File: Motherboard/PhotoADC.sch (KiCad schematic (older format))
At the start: 28 parts

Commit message: Moving along
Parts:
- removed D?: LED, symbol LED
- removed P?: CONN_02X12, symbol CONN_02X12
- added D501: GREEN_LED, LEDs:LED_0805, symbol LED
- added P501, P502, P503, P504: CONN_01X03, moboFootprints:3POS_Header_TEConn_6.35mm_pitch, symbol CONN_01X03
- U501: renamed from U?; footprint (none) -> Housings_SSOP:TSSOP-38_4.4x9.7mm_Pitch0.5mm
- gave numbers to parts that had none: 23
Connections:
- wire segments 58 -> 54

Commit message: Final edits -- awaiting review before sending out
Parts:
- removed C507: 1uF, symbol C
- removed C514: 10nF, symbol C
- removed C515: 2.2uF, symbol C
- removed D501: GREEN_LED, LEDs:LED_0805, symbol LED
- removed R504: 300, symbol R
- removed U503: LP2985-N, symbol LP2985-N
- U501: footprint (none) -> Housings_SSOP:TSSOP-38_4.4x9.7mm_Pitch0.5mm
- U502: footprint (none) -> TO_SOT_Packages_SMD:SOT-23-5_HandSoldering
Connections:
- net GND: now also C508.1, C509.1, C510.1, C511.1, C512.1, C513.1, U504.4 (GND)

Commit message: computer is dying
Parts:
- added R504: 0, Resistors_SMD:R_0805_HandSoldering, symbol R
- R501: footprint (none) -> Resistors_SMD:R_0805_HandSoldering
- R502: footprint (none) -> Resistors_SMD:R_0603_HandSoldering
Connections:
- net at R502.2, U502.1 (Vout): now also R504.1; no longer U502.4 (-)
- new net: R504.2, U502.4 (-)
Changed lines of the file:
@@
 MUX_DATA
 $Comp
-L GND #PWR030
+L GND #PWR513
 U 1 1 59280857
 P 9900 3050
-F 0 "#PWR030" H 9900 2800 50  0001 C CNN
+F 0 "#PWR513" H 9900 2800 50  0001 C CNN
 F 1 "GND" H 9900 2900 50  0000 C CNN
 F 2 "" H 9900 3050 50  0000 C CNN
@@
 $EndComp
 $Comp
-L +5V #PWR031
+L +5V #PWR502
 U 1 1 5928085D
 P 9900 700
-F 0 "#PWR031" H 9900 550 50  0001 C CNN
+F 0 "#PWR502" H 9900 550 50  0001 C CNN
 F 1 "+5V" H 9900 840 50  0000 C CNN
 F 2 "" H 9900 700 50  0000 C CNN
@@
 $EndComp
 $Comp
-L +5V #PWR032
+L +5V #PWR501
 U 1 1 59280863
 P 9700 700
-F 0 "#PWR032" H 9700 550 50  0001 C CNN
+F 0 "#PWR501" H 9700 550 50  0001 C CNN
 F 1 "+5V" H 9700 840 50  0000 C CNN
 F 2 "" H 9700 700 50  0000 C CNN
@@
 $EndComp
 $Comp
-L GND #PWR033
+L GND #PWR509
 U 1 1 5928087F
 P 8850 1750
-F 0 "#PWR033" H 8850 1500 50  0001 C CNN
+F 0 "#PWR509" H 8850 1500 50  0001 C CNN
 F 1 "GND" H 8850 1600 50  0000 C CNN
 F 2 "" H 8850 1750 50  0000 C CNN
@@
 $EndComp
 $Comp
-L GND #PWR034
+L GND #PWR510
 U 1 1 5928088C
 P 10650 1800
-F 0 "#PWR034" H 10650 1550 50  0001 C CNN
+F 0 "#PWR510" H 10650 1550 50  0001 C CNN
 F 1 "GND" H 10650 1650 50  0000 C CNN
 F 2 "" H 10650 1800 50  0000 C CNN
@@
 $EndComp
 $Comp
-L +5V #PWR035
+L +5V #PWR514
 U 1 1 5928089C
 P 9300 4500
-F 0 "#PWR035" H 9300 4350 50  0001 C CNN
+F 0 "#PWR514" H 9300 4350 50  0001 C CNN
 F 1 "+5V" H 9300 4640 50  0000 C CNN
 F 2 "" H 9300 4500 50  0000 C CNN
@@
 $EndComp
 $Comp
-L GND #PWR036
+L GND #PWR516
 U 1 1 592808A9
 P 9300 5350
-F 0 "#PWR036" H 9300 5100 50  0001 C CNN
+F 0 "#PWR516" H 9300 5100 50  0001 C CNN
 F 1 "GND" H 9300 5200 50  0000 C CNN
 F 2 "" H 9300 5350 50  0000 C CNN
@@
 $EndComp
 $Comp
-L GND #PWR037
+L GND #PWR515
 U 1 1 592808AF
 P 9750 4650
-F 0 "#PWR037" H 9750 4400 50  0001 C CNN
+F 0 "#PWR515" H 9750 4400 50  0001 C CNN
 F 1 "GND" H 9750 4500 50  0000 C CNN
 F 2 "" H 9750 4650 50  0000 C CNN
@@
 F 0 "R502" V 10180 4950 50  0000 C CNN
 F 1 "100" V 10100 4950 50  0000 C CNN
-F 2 "" V 10030 4950 50  0001 C CNN
+F 2 "Resistors_SMD:R_0603_HandSoldering" V 10030 4950 50  0001 C CNN
 F 3 "" H 10100 4950 50  0000 C CNN
 	1    10100 4950
@@
 F 0 "R501" V 8680 4900 50  0000 C CNN
 F 1 "0" V 8600 4900 50  0000 C CNN
-F 2 "" V 8530 4900 50  0001 C CNN
+F 2 "Resistors_SMD:R_0805_HandSoldering" V 8530 4900 50  0001 C CNN
 F 3 "" H 8600 4900 50  0000 C CNN
 	1    8600 4900
@@
 $EndComp
 $Comp
-L +5V #PWR038
+L +5V #PWR517
 U 1 1 59280900
 P 3300 6050
-F 0 "#PWR038" H 3300 5900 50  0001 C CNN
+F 0 "#PWR517" H 3300 5900 50  0001 C CNN
 F 1 "+5V" H 3300 6190 50  0000 C CNN
 F 2 "" H 3300 6050 50  0000 C CNN
@@
 NoConn ~ 6350 1750
 $Comp
-L +5V #PWR039
+L +5V #PWR507
 U 1 1 592A5C75
 P 700 1700
-F 0 "#PWR039" H 700 1550 50  0001 C CNN
+F 0 "#PWR507" H 700 1550 50  0001 C CNN
 F 1 "+5V" H 700 1840 50  0000 C CNN
 F 2 "" H 700 1700 50  0000 C CNN
@@
 $EndComp
 $Comp
-L +5V #PWR040
+L +5V #PWR503
 U 1 1 592A5D71
 P 700 1150
-F 0 "#PWR040" H 700 1000 50  0001 C CNN
+F 0 "#PWR503" H 700 1000 50  0001 C CNN
 F 1 "+5V" H 700 1290 50  0000 C CNN
 F 2 "" H 700 1150 50  0000 C CNN
@@
 $EndComp
 $Comp
-L +5V #PWR041
+L +5V #PWR508
 U 1 1 592A5DDE
 P 2550 1700
-F 0 "#PWR041" H 2550 1550 50  0001 C CNN
+F 0 "#PWR508" H 2550 1550 50  0001 C CNN
 F 1 "+5V" H 2550 1840 50  0000 C CNN
 F 2 "" H 2550 1700 50  0000 C CNN
@@
 $EndComp
 $Comp
-L +5V #PWR042
+L +5V #PWR504
 U 1 1 592A5DE5
 P 2550 1150
-F 0 "#PWR042" H 2550 1000 50  0001 C CNN
+F 0 "#PWR504" H 2550 1000 50  0001 C CNN
 F 1 "+5V" H 2550 1290 50  0000 C CNN
 F 2 "" H 2550 1150 50  0000 C CNN
@@
 Wire Wire Line
 	9100 4850 9100 4200
-Wire Wire Line
-	9100 4200 9950 4200
 Wire Wire Line
 	9950 4200 9950 4950
@@
 CH3
 $Comp
-L GND #PWR043
+L GND #PWR506
 U 1 1 592A6F6A
 P 2000 1350
-F 0 "#PWR043" H 2000 1100 50  0001 C CNN
+F 0 "#PWR506" H 2000 1100 50  0001 C CNN
 F 1 "GND" H 2000 1200 50  0000 C CNN
 F 2 "" H 2000 1350 50  0000 C CNN
@@
 $EndComp
 $Comp
-L GND #PWR044
+L GND #PWR512
 U 1 1 592A6FD0
 P 2000 1900
-F 0 "#PWR044" H 2000 1650 50  0001 C CNN
+F 0 "#PWR512" H 2000 1650 50  0001 C CNN
 F 1 "GND" H 2000 1750 50  0000 C CNN
 F 2 "" H 2000 1900 50  0000 C CNN
@@
 $EndComp
 $Comp
-L GND #PWR045
+L GND #PWR505
 U 1 1 592A70ED
 P 1150 1350
-F 0 "#PWR045" H 1150 1100 50  0001 C CNN
+F 0 "#PWR505" H 1150 1100 50  0001 C CNN
 F 1 "GND" H 1150 1200 50  0000 C CNN
 F 2 "" H 1150 1350 50  0000 C CNN
@@
 $EndComp
 $Comp
-L GND #PWR046
+L GND #PWR511
 U 1 1 592A714C
 P 1150 1900
-F 0 "#PWR046" H 1150 1650 50  0001 C CNN
+F 0 "#PWR511" H 1150 1650 50  0001 C CNN
 F 1 "GND" H 1150 1750 50  0000 C CNN
 F 2 "" H 1150 1900 50  0000 C CNN
@@
 Connection ~ 4000 6850
 $Comp
-L GND #PWR047
+L GND #PWR518
 U 1 1 595D7156
 P 4450 6850
-F 0 "#PWR047" H 4450 6600 50  0001 C CNN
+F 0 "#PWR518" H 4450 6600 50  0001 C CNN
 F 1 "GND" H 4450 6700 50  0000 C CNN
 F 2 "" H 4450 6850 50  0000 C CNN
@@
 	1    0    0    -1
 $EndComp
+$Comp
+L R R504
+U 1 1 5962A104
+P 9500 4200
+F 0 "R504" V 9580 4200 50  0000 C CNN
+F 1 "0" V 9500 4200 50  0000 C CNN
+F 2 "Resistors_SMD:R_0805_HandSoldering" V 9430 4200 50  0001 C CNN
+F 3 "" H 9500 4200 50  0000 C CNN
+	1    9500 4200
+	0    1    1    0
+$EndComp
+Wire Wire Line
+	9100 4200 9350 4200
+Wire Wire Line
+	9650 4200 9950 4200
 $EndSCHEMATC

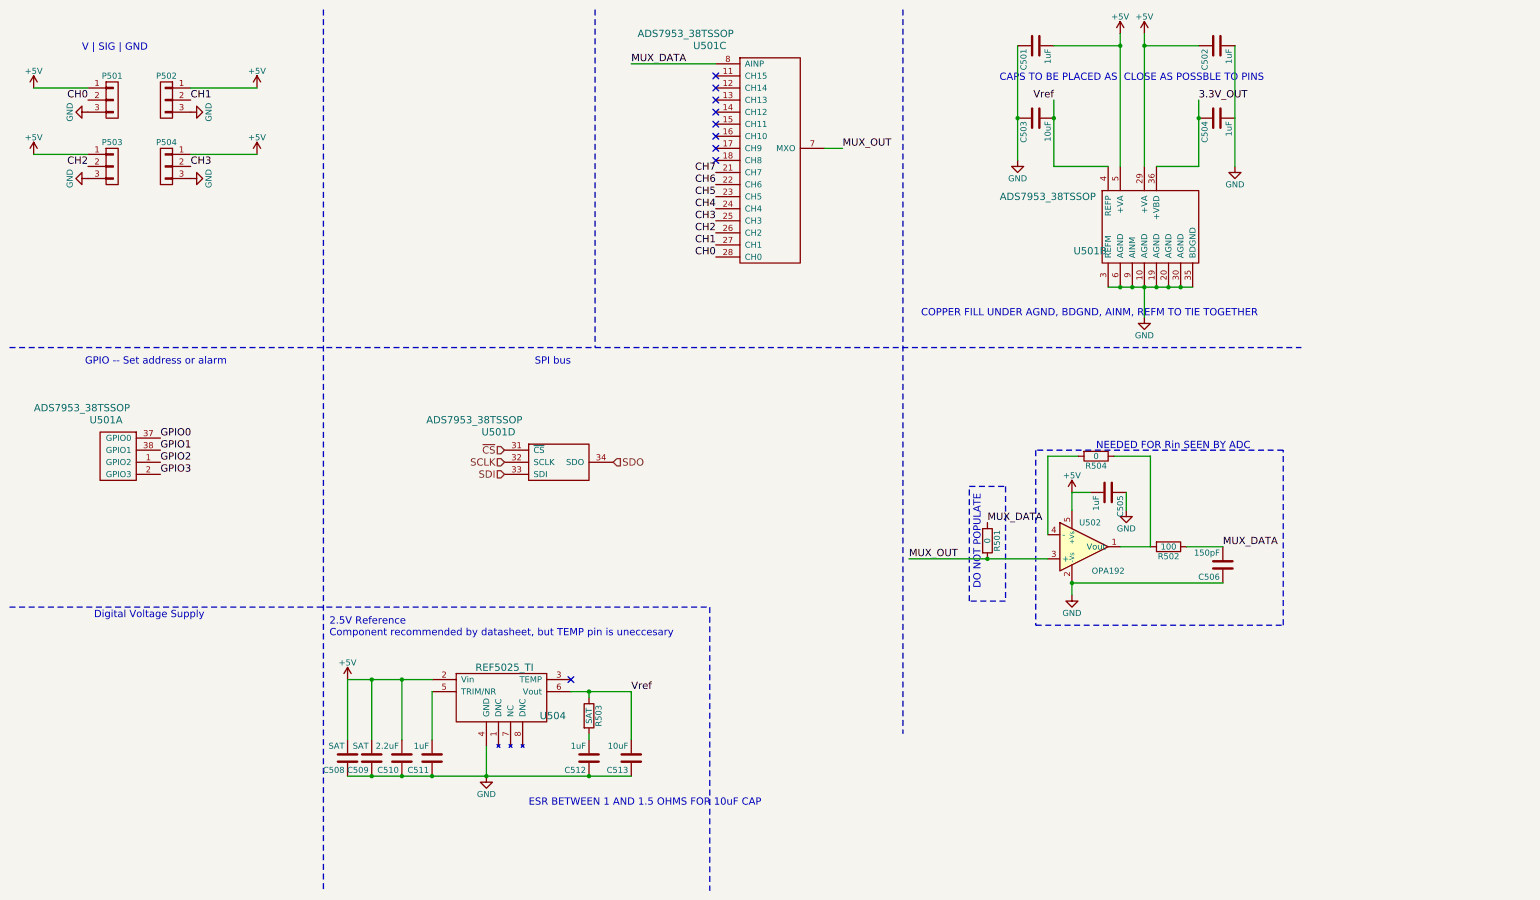
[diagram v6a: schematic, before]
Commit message: Mobo Version 2.1 Added Silk scren Ground Plane Cleanup Pinout changes on Beaglebone Headers, need to modify cabeling from V2.0 and earlier Added power sequencing for ADCs Removed Y3 ADC Removed TI Battery Board I2C lines More 5V connectors on Board Adjusted ADC Connecter pinout to match interface modules
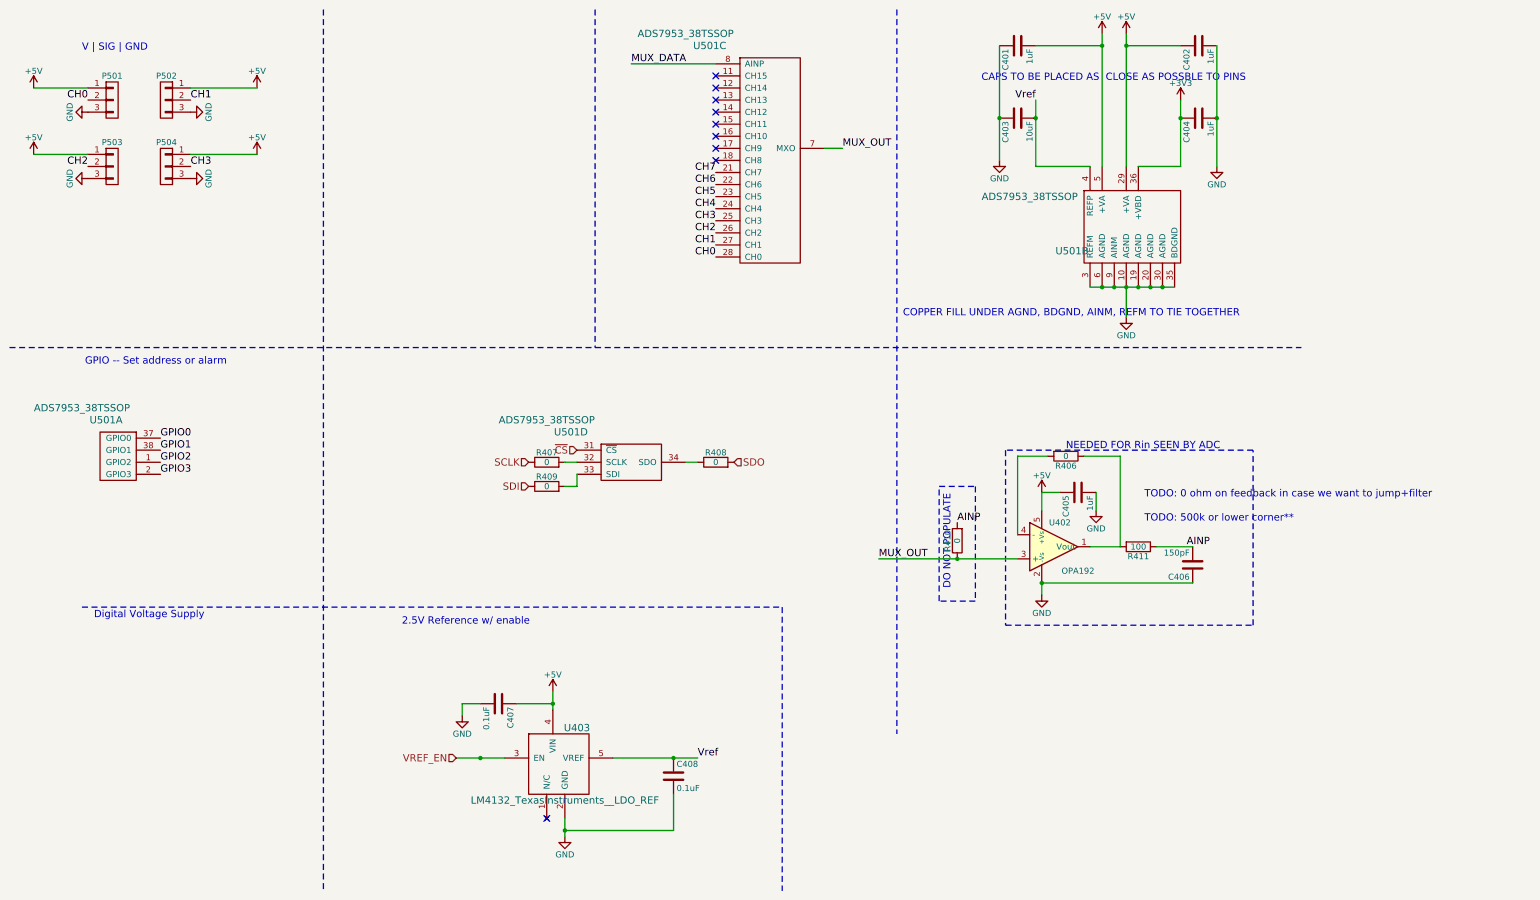
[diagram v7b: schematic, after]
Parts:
- removed C501, C502, C504, C505, C511, C512: 1uF, symbol C
- removed C503, C513: 10uF, symbol C
- removed C506: 150pF, symbol C
- removed C508, C509: SAT, symbol C
- removed C510: 2.2uF, symbol C
- removed R501, R504: 0, Resistors_SMD:R_0805_HandSoldering, symbol R
- removed R502: 100, Resistors_SMD:R_0603_HandSoldering, symbol R
- removed R503: SAT, symbol R
- removed U502: OPA192, TO_SOT_Packages_SMD:SOT-23-5_HandSoldering, symbol OPA656
- removed U504: REF5025_TI, symbol REF2025_TI
- added C401, C402, C404, C405: 1uF, Capacitors_SMD:C_0603_HandSoldering, symbol C
- added C403: 10uF, Capacitors_SMD:C_0603_HandSoldering, symbol C
- added C406: 150pF, Capacitors_SMD:C_0603_HandSoldering, symbol C
- added C407, C408: 0.1uF, Capacitors_SMD:C_0805_HandSoldering, symbol C
- added R406, R407, R408, R409, R410: 0, Resistors_SMD:R_0805_HandSoldering, symbol R
- added R411: 100, Resistors_SMD:R_0603_HandSoldering, symbol R
- added U402: OPA192, TO_SOT_Packages_SMD:SOT-23-5_HandSoldering, symbol OPA656
- added U403: LM4132_TexasInstruments__LDO_REF, TO_SOT_Packages_SMD:SOT-23-5_HandSoldering, symbol LM4132_TexasInstruments__LDO_REF
- U501: Digikey P/N (none) -> 296-23504-5-ND; Mfr P/N (none) -> ADS7953SBDBT
- U501: footprint Housings_SSOP:TSSOP-38_4.4x9.7mm_Pitch0.5mm -> moboFootprints:TSSOP-38_4.4x9.7mm_Pitch0.5mm
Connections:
- net +5V: now also C401.2, C402.1, C405.1, C407.1, U402.5 (+Vs), U403.4 (VIN)
- net GND: now also C401.1, C402.2, C403.1, C404.2, C405.2, C406.1, C407.2, C408.2, U402.2 (-Vs), U403.2 (GND)
- net MUX_OUT: now also R410.1, U402.3 (+)
- net SCLK: now also R407.1; no longer U501.32 (SCLK)
- net SDI: now also R409.1; no longer U501.33 (SDI)
- net SDO: now also R408.2; no longer U501.34 (SDO)
- net Vref: now also C403.2, C408.1, U403.5 (VREF)
- net 3.3V_OUT renamed +3V3
- net +3V3: now also C404.1
- new net: R406.1, R411.2, U402.1 (Vout)
- new net: R406.2, U402.4 (-)
- new net: R407.2, U501.32 (SCLK)
- new net: R409.2, U501.33 (SDI)
- new net: R408.1, U501.34 (SDO)
- new net AINP: C406.2, R410.2, R411.1
- new net VREF_EN: U403.3 (EN)
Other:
- note added: "2.5V Reference w/ enable\n\n"
- note added: "TODO: 0 ohm on feedback in case we want to jump+filter"
- note added: "TODO: 500k or lower corner**"
- note removed: "2.5V Reference\nComponent recommended by datasheet, but TEMP pin is uneccesary\n"
- note removed: "ESR BETWEEN 1 AND 1.5 OHMS FOR 10uF CAP\n\n"
- note removed: "SPI bus"
